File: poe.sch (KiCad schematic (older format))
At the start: 56 parts, among them J201 Screw_Terminal_01x04, J202 Screw_Terminal_01x02, Q201 FDC2512, T201 HR051067, U201 TPS23753A, U202 TL431D, U203 EL3H7A

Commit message: Added CO sensor
Carbon Monoxide Sensor layout
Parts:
- Q201: symbol Transistor_FET:FDC2512 -> SD1-rescue:FDC2512-Transistor_FET
- T201: symbol mylib:HR051067 -> SD1-rescue:HR051067-mylib
- U201: symbol mylib:TPS23753A -> SD1-rescue:TPS23753A-mylib
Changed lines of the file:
@@
 $EndDescr
 $Comp
-L mylib:HR051067 T?
+L SD1-rescue:HR051067-mylib T?
 U 1 1 5F85962B
 P 10350 4400
@@
 $EndComp
 $Comp
-L mylib:TPS23753A U201
+L SD1-rescue:TPS23753A-mylib U201
 U 1 1 5F6FB03A
 P 7000 5400
@@
 $EndComp
 $Comp
-L Transistor_FET:FDC2512 Q201
+L SD1-rescue:FDC2512-Transistor_FET Q201
 U 1 1 5F7D1B09
 P 9250 5500

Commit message: Minor cleanup
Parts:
- Q201: symbol SD1-rescue:FDC2512-Transistor_FET -> Transistor_FET:FDC2512
- T201: symbol SD1-rescue:HR051067-mylib -> mylib:HR051067
- U201: symbol SD1-rescue:TPS23753A-mylib -> mylib:TPS23753A
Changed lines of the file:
@@
 $EndDescr
 $Comp
-L SD1-rescue:HR051067-mylib T?
+L mylib:HR051067 T?
 U 1 1 5F85962B
 P 10350 4400
@@
 $EndComp
 $Comp
-L SD1-rescue:TPS23753A-mylib U201
+L mylib:TPS23753A U201
 U 1 1 5F6FB03A
 P 7000 5400
@@
 $EndComp
 $Comp
-L SD1-rescue:FDC2512-Transistor_FET Q201
+L Transistor_FET:FDC2512 Q201
 U 1 1 5F7D1B09
 P 9250 5500

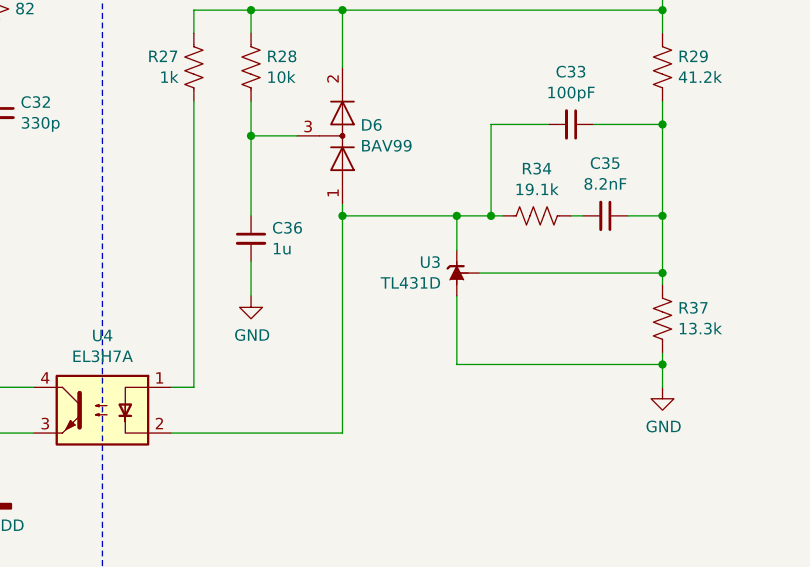
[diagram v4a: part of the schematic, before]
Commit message: Minor part picking and annotation
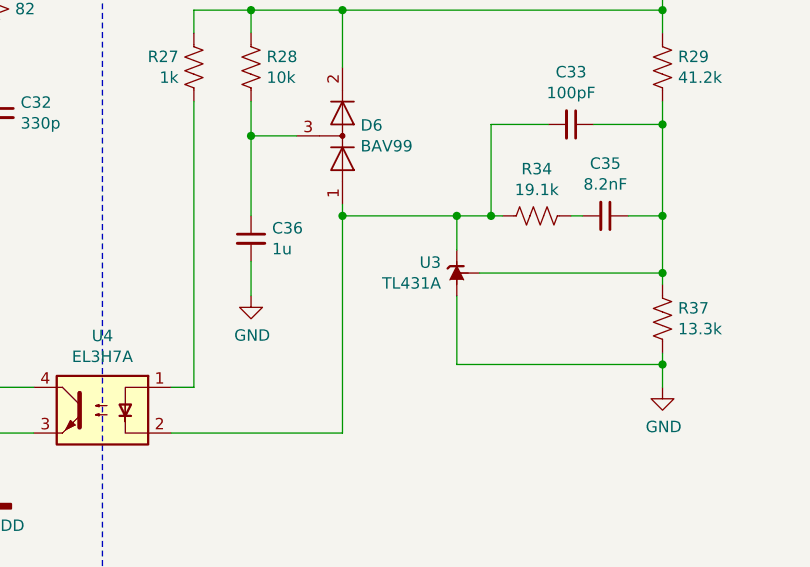
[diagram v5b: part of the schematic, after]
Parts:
- R211: Digikey (none) -> 311-1.00KHRCT-ND; Error 1% -> (none); MPN (none) -> RC0603FR-071KL; Note (none) -> RES SMD 1K OHM 1% 1/10W 0603
- R215: footprint Resistor_SMD:R_0805_2012Metric -> Resistor_SMD:R_0603_1608Metric; Digikey 311-1.0KARCT-ND -> 311-1.00KHRCT-ND; Error 5% -> (none); LCSC C100046 -> (none); MPN RC0805JR-071KL -> RC0603FR-071KL; Note RES SMD 1K OHM 5% 1/10W 0805 -> RES SMD 1K OHM 1% 1/10W 0603; Power 1/10W -> (none); Size 0805 -> (none)
- U201: footprint (none) -> Package_SO:TSSOP-14_4.4x5mm_P0.65mm; Digikey (none) -> 296-39365-1-ND; LCSC (none) -> C92115; MPN (none) -> TPS23753APWR; Manufacturer (none) -> Texas Instruments; Note (none) -> IC POE CNTRL 1 CHANNEL 14TSSOP
- U202: value TL431D -> TL431A; footprint Package_SO:SOIC-8_3.9x4.9mm_P1.27mm -> Package_TO_SOT_SMD:SOT-23; Digikey (none) -> 296-17328-1-ND; LCSC (none) -> C113312; MPN (none) -> TL431ACDBZR; Manufacturer (none) -> Texas Instruments; Note (none) -> IC VREF SHUNT 36V 1% SOT23-3
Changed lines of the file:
@@
 AR Path="/5FCEDB09/5FAC6B33/5F85964F" Ref="U3"  Part="1"
 F 0 "U3" V 11946 6681 50  0000 R CNN
-F 1 "TL431D" V 11855 6681 50  0000 R CNN
-F 2 "Package_SO:SOIC-8_3.9x4.9mm_P1.27mm" H 11900 6500 50  0001 C CIN
+F 1 "TL431A" V 11855 6681 50  0000 R CNN
+F 2 "Package_TO_SOT_SMD:SOT-23" H 11900 6500 50  0001 C CIN
 F 3 "http://www.ti.com/lit/ds/symlink/tl431.pdf" H 11900 6750 50  0001 C CIN
+F 4 "296-17328-1-ND" H 11900 6750 50  0001 C CNN "Digikey"
+F 5 "C113312" H 11900 6750 50  0001 C CNN "LCSC"
+F 6 "TL431ACDBZR" H 11900 6750 50  0001 C CNN "MPN"
+F 7 "Texas Instruments" H 11900 6750 50  0001 C CNN "Manufacturer"
+F 8 "IC VREF SHUNT 36V 1% SOT23-3" H 11900 6750 50  0001 C CNN "Note"
 	1    11900 6750
 	0    1    -1   0
@@
 F 0 "U2" H 6975 5965 50  0000 C CNN
 F 1 "TPS23753A" H 6975 5874 50  0000 C CNN
-F 2 "" H 6950 5850 50  0001 C CNN
+F 2 "Package_SO:TSSOP-14_4.4x5mm_P0.65mm" H 6950 5850 50  0001 C CNN
 F 3 "" H 6950 5850 50  0001 C CNN
+F 4 "296-39365-1-ND" H 7000 5400 50  0001 C CNN "Digikey"
+F 5 "C92115" H 7000 5400 50  0001 C CNN "LCSC"
+F 6 "TPS23753APWR" H 7000 5400 50  0001 C CNN "MPN"
+F 7 "Texas Instruments" H 7000 5400 50  0001 C CNN "Manufacturer"
+F 8 "IC POE CNTRL 1 CHANNEL 14TSSOP" H 7000 5400 50  0001 C CNN "Note"
 	1    7000 5400
 	-1   0    0    -1
@@
 F 0 "R31" H 13818 6096 50  0000 L CNN
 F 1 "1k" H 13818 6005 50  0000 L CNN
-F 2 "Resistor_SMD:R_0805_2012Metric" H 13750 6050 50  0001 C CNN
-F 3 "~" H 13750 6050 50  0001 C CNN
-F 4 "1/10W" H 13750 6050 50  0001 C CNN "Power"
-F 5 "5%" H 13750 6050 50  0001 C CNN "Error"
-F 6 "0805" H 13750 6050 50  0001 C CNN "Size"
-F 7 "RES SMD 1K OHM 5% 1/10W 0805" H 13750 6050 50  0001 C CNN "Note"
-F 8 "311-1.0KARCT-ND" H 13750 6050 50  0001 C CNN "Digikey"
-F 9 "C100046" H 13750 6050 50  0001 C CNN "LCSC"
-F 10 "RC0805JR-071KL" H 13750 6050 50  0001 C CNN "MPN"
+F 2 "Resistor_SMD:R_0603_1608Metric" H 13750 6050 50  0001 C CNN
+F 3 "RES SMD 1K OHM 1% 1/10W 0603" H 13750 6050 50  0001 C CNN
+F 4 "" H 13750 6050 50  0001 C CNN "Power"
+F 5 "" H 13750 6050 50  0001 C CNN "Error"
+F 6 "" H 13750 6050 50  0001 C CNN "Size"
+F 7 "RES SMD 1K OHM 1% 1/10W 0603" H 13750 6050 50  0001 C CNN "Note"
+F 8 "311-1.00KHRCT-ND" H 13750 6050 50  0001 C CNN "Digikey"
+F 9 "" H 13750 6050 50  0001 C CNN "LCSC"
+F 10 "RC0603FR-071KL" H 13750 6050 50  0001 C CNN "MPN"
 	1    13750 6050
 	1    0    0    -1
@@
 F 3 "~" H 10750 5850 50  0001 C CNN
 F 4 "1/16W" H 10750 5850 50  0001 C CNN "Power"
-F 5 "1%" H 10750 5850 50  0001 C CNN "Error"
+F 5 "" H 10750 5850 50  0001 C CNN "Error"
 F 6 "0603" H 10750 5850 50  0001 C CNN "Size"
+F 7 "311-1.00KHRCT-ND" H 10750 5850 50  0001 C CNN "Digikey"
+F 8 "RC0603FR-071KL" H 10750 5850 50  0001 C CNN "MPN"
+F 9 "RES SMD 1K OHM 1% 1/10W 0603" H 10750 5850 50  0001 C CNN "Note"
 	1    10750 5850
 	1    0    0    -1

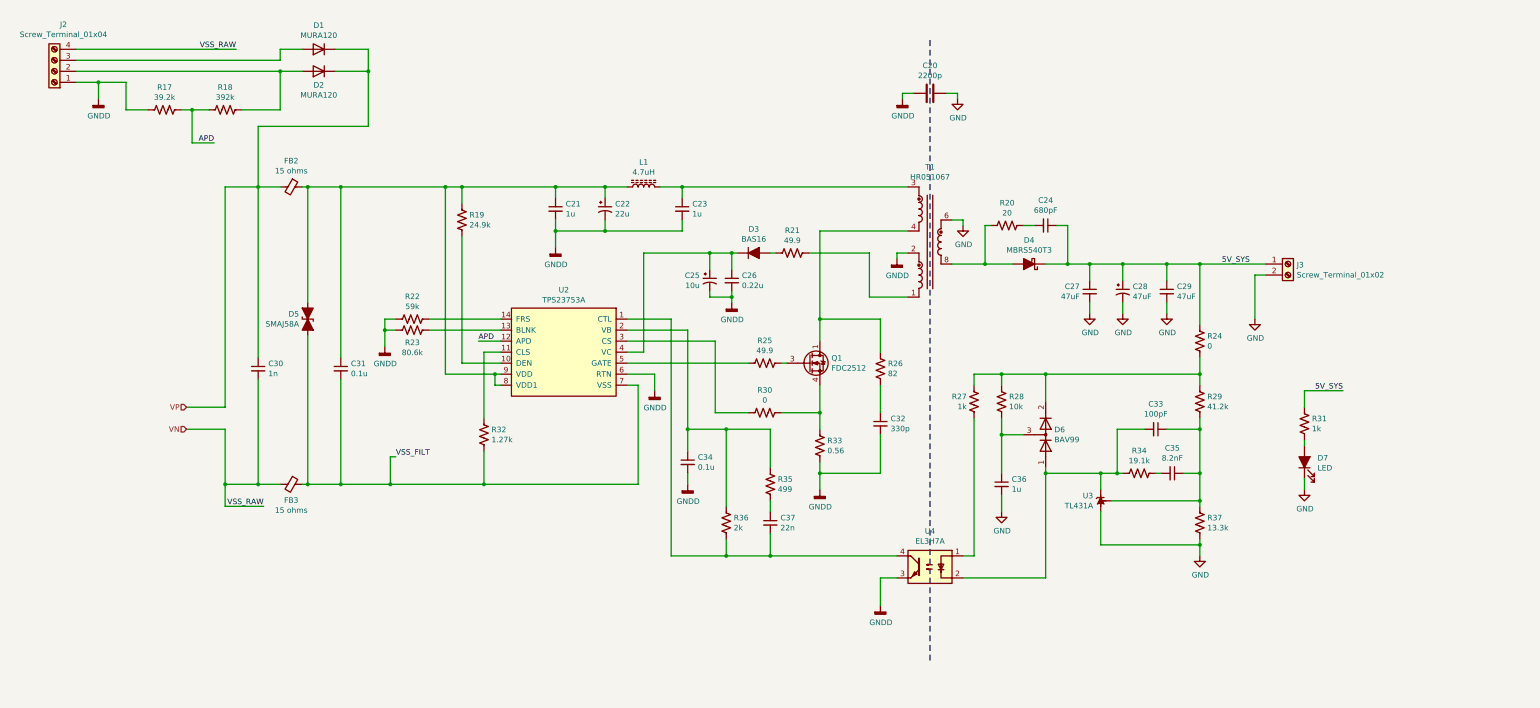
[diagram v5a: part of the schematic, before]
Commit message: Major power changes
Added 5v boost, 3.3 buck, ideal diode circuits.
Poe: added barrel jacks
Smoke: general cleanup
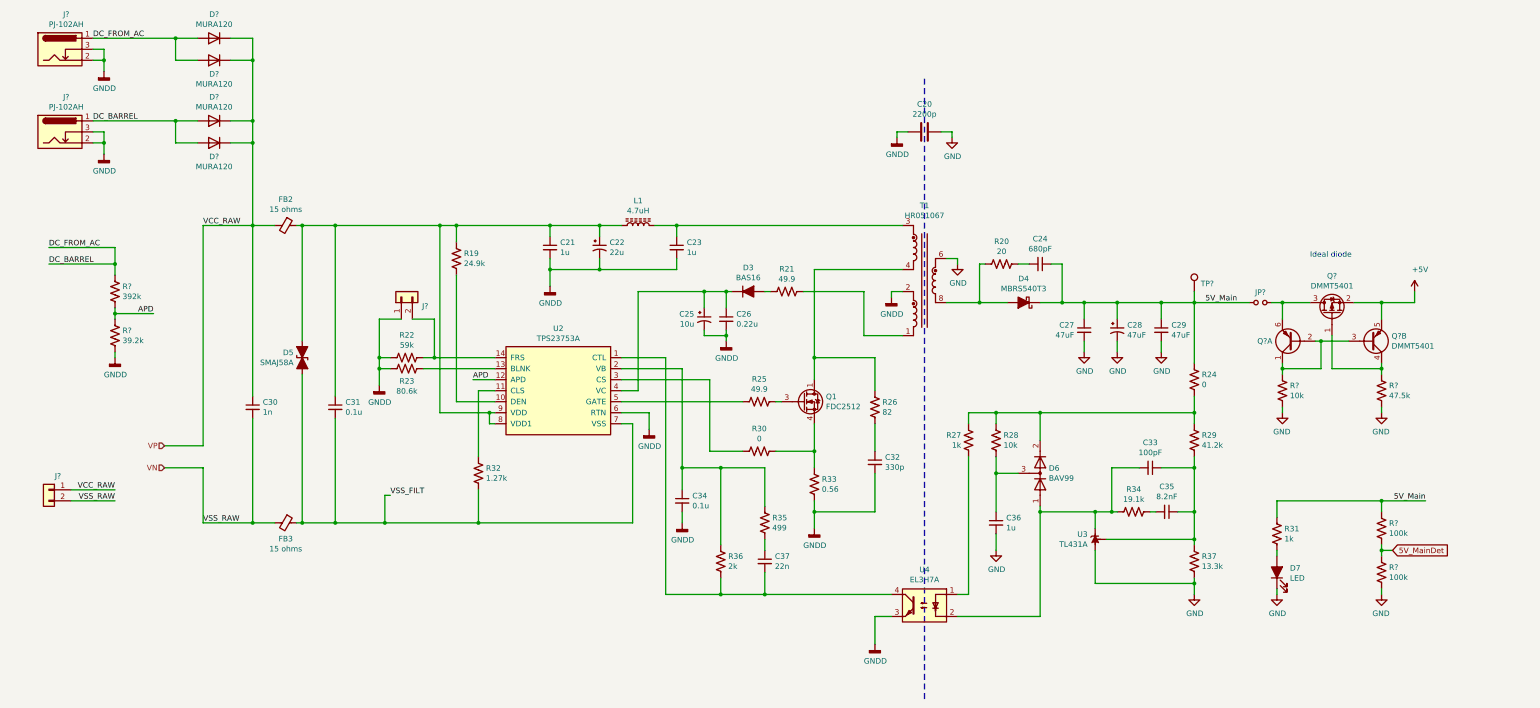
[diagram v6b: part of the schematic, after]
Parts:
- removed D201, D202: MURA120, Diode_SMD:D_SMA, symbol Device:D
- removed J201: Screw_Terminal_01x04, symbol Connector:Screw_Terminal_01x04
- removed J202: Screw_Terminal_01x02, symbol Connector:Screw_Terminal_01x02
- removed R201: 39.2k, Resistor_SMD:R_0603_1608Metric, symbol Device:R_US
- removed R202: 392k, Resistor_SMD:R_0603_1608Metric, symbol Device:R_US
- added D? (x4): MURA120, Diode_SMD:D_SMA, symbol Device:D
- added J? (x2): PJ-102AH, Connector_BarrelJack:BarrelJack_CUI_PJ-102AH_Horizontal, symbol Connector:Barrel_Jack_Switch
- added J? (x2): Conn_01x02, Connector_PinSocket_2.54mm:PinSocket_1x02_P2.54mm_Vertical, symbol Connector_Generic:Conn_01x02
- added JP?: Jumper_NO_Small, Jumper:SolderJumper-2_P1.3mm_Open_TrianglePad1.0x1.5mm, symbol Device:Jumper_NO_Small
- added Q?: DMMT5401, Package_TO_SOT_SMD:SOT-23-6, symbol Device:Q_PMOS_GSD
- added Q? (x2): DMMT5401, Package_TO_SOT_SMD:SOT-23-6, symbol Device:Q_DUAL_PNP_PNP_C1B1B2C2E2E1
- added R? (x2): 100k, Resistor_SMD:R_0603_1608Metric, symbol Device:R_US
- added R?: 39.2k, Resistor_SMD:R_0603_1608Metric, symbol Device:R_US
- added R?: 392k, Resistor_SMD:R_0603_1608Metric, symbol Device:R_US
- added R?: 10k, Resistor_SMD:R_0603_1608Metric, symbol Device:R_US
- added R?: 47.5k, Resistor_SMD:R_0603_1608Metric, symbol Device:R_US
- added TP?: TestPoint, Connector_PinSocket_2.54mm:PinSocket_1x01_P2.54mm_Vertical, symbol Connector:TestPoint
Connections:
- net APD: now also R?.1, R?.2
- net GND: now also R?.1, R?.1, R?.2
- net GNDD: now also J?.1 (Pin_1), J?.2, J?.2, J?.3, J?.3, R?.2
- net VN: now also J?.2 (Pin_2)
- net VP: now also D?.1 (K), D?.1 (K), D?.1 (K), D?.1 (K), J?.1 (Pin_1)
- net at R206.1, U201.14 (FRS): now also J?.2 (Pin_2)
- net 5V_SYS renamed 5V_Main
- net 5V_Main: now also JP?.1, R?.2, TP?.1
- new net: JP?.2, Q?.3 (D), Q?.6 (E1)
- new net: Q?.1 (G), Q?.4 (C2), R?.2
- new net: Q?.1 (C1), Q?.2 (B1), Q?.3 (B2), R?.1
- new net +5V: Q?.2 (S), Q?.5 (E2)
- new net 5V_MainDet: R?.1, R?.2
- new net DC_BARREL: D?.2 (A), D?.2 (A), D?.2 (A), D?.2 (A), J?.1, J?.1, R?.1
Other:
- note added: "Ideal diode"
- moved on the sheet: C20, C21, C22, C23, C24, C25, C26, C27, C28, C29, C30, C31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

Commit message: Continue part picking
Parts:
- D203: footprint (none) -> Diode_SMD:D_SOT-23_ANK; Digikey (none) -> BAS16-FDICT-ND; LCSC (none) -> C69162*; MPN (none) -> BAS16-7-F; Note (none) -> DIODE GEN PURP 75V 200MA SOT23-3
- D204: LCSC (none) -> C31849; MPN (none) -> MBRS540T3G; Note (none) -> RECTIFIER DIODE, SCHOTTKY, 5A, 4
- D206: Digikey (none) -> 1727-2914-1-ND; LCSC (none) -> C152481; MPN (none) -> BAV99,215; Note (none) -> BAV99 switching diode, generic
- D207: value LED -> LED_ALT; footprint (none) -> LED_SMD:LED_0603_1608Metric; Digikey (none) -> 732-4978-1-ND; LCSC (none) -> C205443; MPN (none) -> 150060RS75000; Note (none) -> LED RED CLEAR 0603 SMD
- FB201, FB202: value 15 ohms -> 10; footprint (none) -> Resistor_SMD:R_0603_1608Metric; LCSC (none) -> C280672; MPN (none) -> PBY160808T-110Y-N; Manufacturer (none) -> Chilisin Elec; Note (none) -> 11Ω @ 100MHz 4A 1 20mΩ 0603 Ferrite Beads
- J301, J302: renamed from J?; LCSC (none) -> C84007
- L201: value 4.7uH -> 4.7u; footprint (none) -> Inductor_SMD:L_Taiyo-Yuden_MD-4040; Current 1.5A -> (none); Digikey (none) -> 587-5994-1-ND; LCSC (none) -> C206284, C326301, C15269; MPN (none) -> SLW4030S4R7MST; Note (none) -> 4.7uH ±20% 2A 60mΩ SMD,4x4x3mm; Resistance 90m -> (none); Size .26x.09in -> (none)
- Q201: value FDC2512 -> FDT86244; footprint Package_TO_SOT_SMD:SuperSOT-6 -> Package_TO_SOT_SMD:SOT-223-3_TabPin2; symbol Transistor_FET:FDC2512 -> Device:Q_NMOS_GDS; Digikey (none) -> FDT86244CT-ND; LCSC (none) -> C489347; MPN (none) -> FDT86244; Note (none) -> MOSFET N-CH 150V 2.8A SOT-223
- gave numbers to parts that had none: 16
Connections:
- net at Q201.2 (D), R210.1, T201.4: no longer Q201.1 (D), Q201.5 (D), Q201.6 (D)
- net at R209.1: now also Q201.1 (G); no longer Q201.3 (G)
- net at R214.1, R217.1: now also Q201.3 (S); no longer Q201.4 (S)

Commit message: Set transformer footprint
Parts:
- T201: footprint (none) -> mylib:HR051067
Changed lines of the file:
@@
 F 0 "T1" H 10300 5431 50  0000 C CNN
 F 1 "HR051067" H 10300 5340 50  0000 C CNN
-F 2 "" H 10300 4750 50  0001 C CNN
+F 2 "mylib:HR051067" H 10300 4750 50  0001 C CNN
 F 3 "" H 10600 4750 50  0001 C CNN
 F 4 "HR051067" H 10300 4750 50  0001 C CNN "MPN"
